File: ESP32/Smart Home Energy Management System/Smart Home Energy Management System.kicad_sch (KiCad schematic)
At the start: 154 parts, among them J1 NEPA, J10 N, J11 PZEM_SIG, J14 USB_C Conn, J15 TRANS 1-OUT, J16 128X64 GLCD, J17 TRANS-IN, J18 TRANS 2-OUT, J19 DISPLAY, J2 INVERTER, J20 LOAD 6, J21 LOAD 5, J22 LOAD 4, J23 LOAD 3, J24 LOAD 2, J25 LOAD 1, J3 CT, J6 PZEM_LOAD, K1 10A RELAY, K10 30A RELAY, K11 30A RELAY, K12 30A RELAY, K13 30A RELAY, K2 30A RELAY, K3 30A RELAY, K4 30A RELAY, K5 30A RELAY, K6 30A RELAY, K7 30A RELAY, K8 30A RELAY, K9 30A RELAY, Q1 UMH3N, Q2 UMH3N, Q3 ULN2803ADWR, Q4 ULN2803ADWR, SW1 RESET, SW2 FLASH, SW3 RotaryEncoder, T1 2220-12V, T2 2220-12V, U1 LM2596S-3.3V, U2 LM2596S-12, U3 ESP32-WROOM, U4 LM2596S-5V, U5 AMS1117-3.3, U6 PCA9555D, U7 CH340C, Y1 12MHz

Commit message: update from home
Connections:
- net D+: now reaches J14.2 (Pin_2), U7.5 (UD+)
- net D-: now reaches J14.3 (Pin_3), U7.6 (UD-)
- net RXN: no longer names the net of J11.3 (Pin_3), JP2.2 (B)
- net TXP: no longer names the net of J11.2 (Pin_2), JP1.2 (B)
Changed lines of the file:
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@@
 	)
 	(junction
-		(at 193.04 69.85)
-		(diameter 0)
-		(color 0 0 0 0)
-	)
-	(junction
 		(at 144.78 62.23)
 		(diameter 0)
@@
 	)
 	(junction
-		(at 200.66 71.12)
-		(diameter 0)
-		(color 0 0 0 0)
-	)
-	(junction
 		(at 191.77 157.48)
 		(diameter 0)
@@
 	(wire
 		(pts
-			(xy 193.04 66.04) (xy 193.04 69.85)
-		)
-		(stroke
-			(width 0)
-			(type default)
-		)
-	)
-	(wire
-		(pts
 			(xy 308.61 111.76) (xy 309.88 111.76)
 		)
@@
 	(wire
 		(pts
-			(xy 200.66 66.04) (xy 200.66 71.12)
-		)
-		(stroke
-			(width 0)
-			(type default)
-		)
-	)
-	(wire
-		(pts
 			(xy 64.77 185.42) (xy 71.12 185.42)
 		)
@@
 	(wire
 		(pts
-			(xy 209.55 261.62) (xy 209.55 271.78)
-		)
-		(stroke
-			(width 0)
-			(type default)
-		)
-	)
-	(wire
-		(pts
 			(xy 135.89 57.15) (xy 135.89 62.23)
 		)
@@
 	(wire
 		(pts
-			(xy 189.23 69.85) (xy 193.04 69.85)
+			(xy 189.23 69.85) (xy 247.65 69.85)
 		)
 		(stroke
@@
 	(wire
 		(pts
+			(xy 209.55 261.62) (xy 209.55 271.78)
+		)
+		(stroke
+			(width 0)
+			(type default)
+		)
+	)
+	(wire
+		(pts
 			(xy 180.34 172.72) (xy 180.34 185.42)
 		)
@@
 	(wire
 		(pts
-			(xy 66.04 266.7) (xy 69.85 266.7)
-		)
-		(stroke
-			(width 0)
-			(type default)
-		)
-	)
-	(wire
-		(pts
 			(xy 245.11 116.84) (xy 264.16 116.84)
 		)
@@
 	(wire
 		(pts
-			(xy 193.04 69.85) (xy 247.65 69.85)
-		)
-		(stroke
-			(width 0)
-			(type default)
-		)
-	)
-	(wire
-		(pts
 			(xy 34.29 48.26) (xy 34.29 49.53)
 		)
@@
 	(wire
 		(pts
+			(xy 62.23 266.7) (xy 69.85 266.7)
+		)
+		(stroke
+			(width 0)
+			(type default)
+		)
+	)
+	(wire
+		(pts
 			(xy 269.24 229.87) (xy 276.86 229.87)
 		)
@@
 		)
 	)
+	(label "D+"
+		(at 195.58 69.85 0)
+		(fields_autoplaced yes)
+		(effects
+			(font
+				(size 1.27 1.27)
+			)
+			(justify left bottom)
+		)
+		(property "Netclass" "DIFF"
+			(at 195.58 71.12 0)
+			(effects
+				(font
+					(size 1.27 1.27)
+					(italic yes)
+				)
+				(justify left)
+			)
+		)
+	)
 	(label "GPIO17"
 		(at 125.73 152.4 180)
@@
 		)
 	)
-	(label "RXN"
-		(at 107.95 158.75 0)
-		(effects
-			(font
-				(size 1.27 1.27)
-			)
-			(justify left bottom)
-		)
-		(property "Netclass" "DIFF"
-			(at 102.616 157.988 0)
-			(effects
-				(font
-					(size 1.27 1.27)
-					(italic yes)
-				)
-				(justify left)
-			)
-		)
-	)
 	(label "INVERTER"
 		(at 300.99 80.01 0)
@@
 	)
 	(label "N"
-		(at 66.04 266.7 0)
+		(at 62.23 266.7 0)
 		(effects
 			(font
@@
 		)
 	)
-	(label "TXP"
-		(at 107.95 156.21 0)
-		(effects
-			(font
-				(size 1.27 1.27)
-			)
-			(justify left bottom)
-		)
-		(property "Netclass" "DIFF"
-			(at 102.616 155.448 0)
-			(effects
-				(font
-					(size 1.27 1.27)
-					(italic yes)
-				)
-				(justify left)
-			)
-		)
-	)
 	(label "DTR"
 		(at 232.41 52.07 180)
@@
 		)
 	)
+	(label "D-"
+		(at 195.58 72.39 0)
+		(effects
+			(font
+				(size 1.27 1.27)
+			)
+			(justify left bottom)
+		)
+		(property "Netclass" "DIFF"
+			(at 190.5 71.374 0)
+			(effects
+				(font
+					(size 1.27 1.27)
+					(italic yes)
+				)
+				(justify left)
+			)
+		)
+	)
 	(label "CT +"
 		(at 64.77 161.29 0)
@@
 		(length 2.54)
 		(shape round)
-		(at 193.04 66.04 0)
-		(fields_autoplaced yes)
-		(effects
-			(font
-				(size 1.27 1.27)
-			)
-			(justify left bottom)
-		)
-		(property "Netclass" "DIFF"
-			(at 193.6496 63.5 0)
-			(effects
-				(font
-					(size 1.27 1.27)
-				)
-				(justify left)
-			)
-		)
-		(property "Component Class" ""
-			(at -35.56 -59.69 0)
-			(effects
-				(font
-					(size 1.27 1.27)
-					(italic yes)
-				)
-			)
-		)
-	)
-	(netclass_flag ""
-		(length 2.54)
-		(shape round)
 		(at 331.47 82.55 0)
 		(fields_autoplaced yes)
@@
 			(effects
 				(font
-					(size 1.27 1.27)
-					(italic yes)
-				)
-			)
-		)
-	)
-	(netclass_flag ""
-		(length 2.54)
-		(shape round)
-		(at 200.66 66.04 0)
-		(fields_autoplaced yes)
-		(effects
-			(font
-				(size 1.27 1.27)
-			)
-			(justify left bottom)
-		)
-		(property "Netclass" "DIFF"
-			(at 201.2696 63.5 0)
-			(effects
-				(font
-					(size 1.27 1.27)
-				)
-				(justify left)
-			)
-		)
-		(property "Component Class" ""
-			(at -27.94 -59.69 0)
-			(effects
-				(font

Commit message: update from home
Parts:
- R13: footprint Resistor_THT:R_Axial_DIN0207_L6.3mm_D2.5mm_P10.16mm_Horizontal -> Resistor_THT:R_Axial_DIN0207_L6.3mm_D2.5mm_P7.62mm_Horizontal
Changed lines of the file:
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@@
 	)
 	(junction
+		(at 215.9 21.59)
+		(diameter 0)
+		(color 0 0 0 0)
+	)
+	(junction
 		(at 331.47 175.26)
 		(diameter 0)
@@
 	)
 	(junction
+		(at 189.23 21.59)
+		(diameter 0)
+		(color 0 0 0 0)
+	)
+	(junction
 		(at 114.3 62.23)
 		(diameter 0)
@@
 	(wire
 		(pts
-			(xy 185.42 21.59) (xy 191.77 21.59)
+			(xy 185.42 21.59) (xy 189.23 21.59)
 		)
 		(stroke
@@
 	(wire
 		(pts
+			(xy 189.23 21.59) (xy 191.77 21.59)
+		)
+		(stroke
+			(width 0)
+			(type default)
+		)
+	)
+	(wire
+		(pts
 			(xy 191.77 88.9) (xy 191.77 91.44)
 		)
@@
 	(wire
 		(pts
+			(xy 215.9 17.78) (xy 215.9 21.59)
+		)
+		(stroke
+			(width 0)
+			(type default)
+		)
+	)
+	(wire
+		(pts
 			(xy 373.38 186.69) (xy 374.65 186.69)
 		)
@@
 	(wire
 		(pts
+			(xy 189.23 19.05) (xy 189.23 21.59)
+		)
+		(stroke
+			(width 0)
+			(type default)
+		)
+	)
+	(wire
+		(pts
 			(xy 139.7 22.86) (xy 144.78 22.86)
 		)
@@
 		(length 2.54)
 		(shape round)
+		(at 189.23 19.05 0)
+		(fields_autoplaced yes)
+		(effects
+			(font
+				(size 1.27 1.27)
+			)
+			(justify left bottom)
+		)
+		(property "Netclass" "PWR"
+			(at 189.8396 16.51 0)
+			(effects
+				(font
+					(size 1.27 1.27)
+				)
+				(justify left)
+			)
+		)
+		(property "Component Class" ""
+			(at 90.17 -2.54 0)
+			(effects
+				(font
+					(size 1.27 1.27)
+					(italic yes)
+				)
+			)
+		)
+	)
+	(netclass_flag ""
+		(length 2.54)
+		(shape round)
 		(at 123.19 53.34 0)
 		(fields_autoplaced yes)
@@
 		(length 2.54)
 		(shape round)
+		(at 215.9 17.78 0)
+		(fields_autoplaced yes)
+		(effects
+			(font
+				(size 1.27 1.27)
+			)
+			(justify left bottom)
+		)
+		(property "Netclass" "PWR"
+			(at 216.5096 15.24 0)
+			(effects
+				(font
+					(size 1.27 1.27)
+				)
+				(justify left)
+			)
+		)
+		(property "Component Class" ""
+			(at 116.84 -3.81 0)
+			(effects
+				(font
+					(size 1.27 1.27)
+					(italic yes)
+				)
+			)
+		)
+	)
+	(netclass_flag ""
+		(length 2.54)
+		(shape round)
 		(at 125.73 76.2 0)
 		(fields_autoplaced yes)
@@
 			)
 		)
-		(property "Footprint" "Resistor_THT:R_Axial_DIN0207_L6.3mm_D2.5mm_P10.16mm_Horizontal"
+		(property "Footprint" "Resistor_THT:R_Axial_DIN0207_L6.3mm_D2.5mm_P7.62mm_Horizontal"
 			(at 107.061 55.372 0)
 			(effects

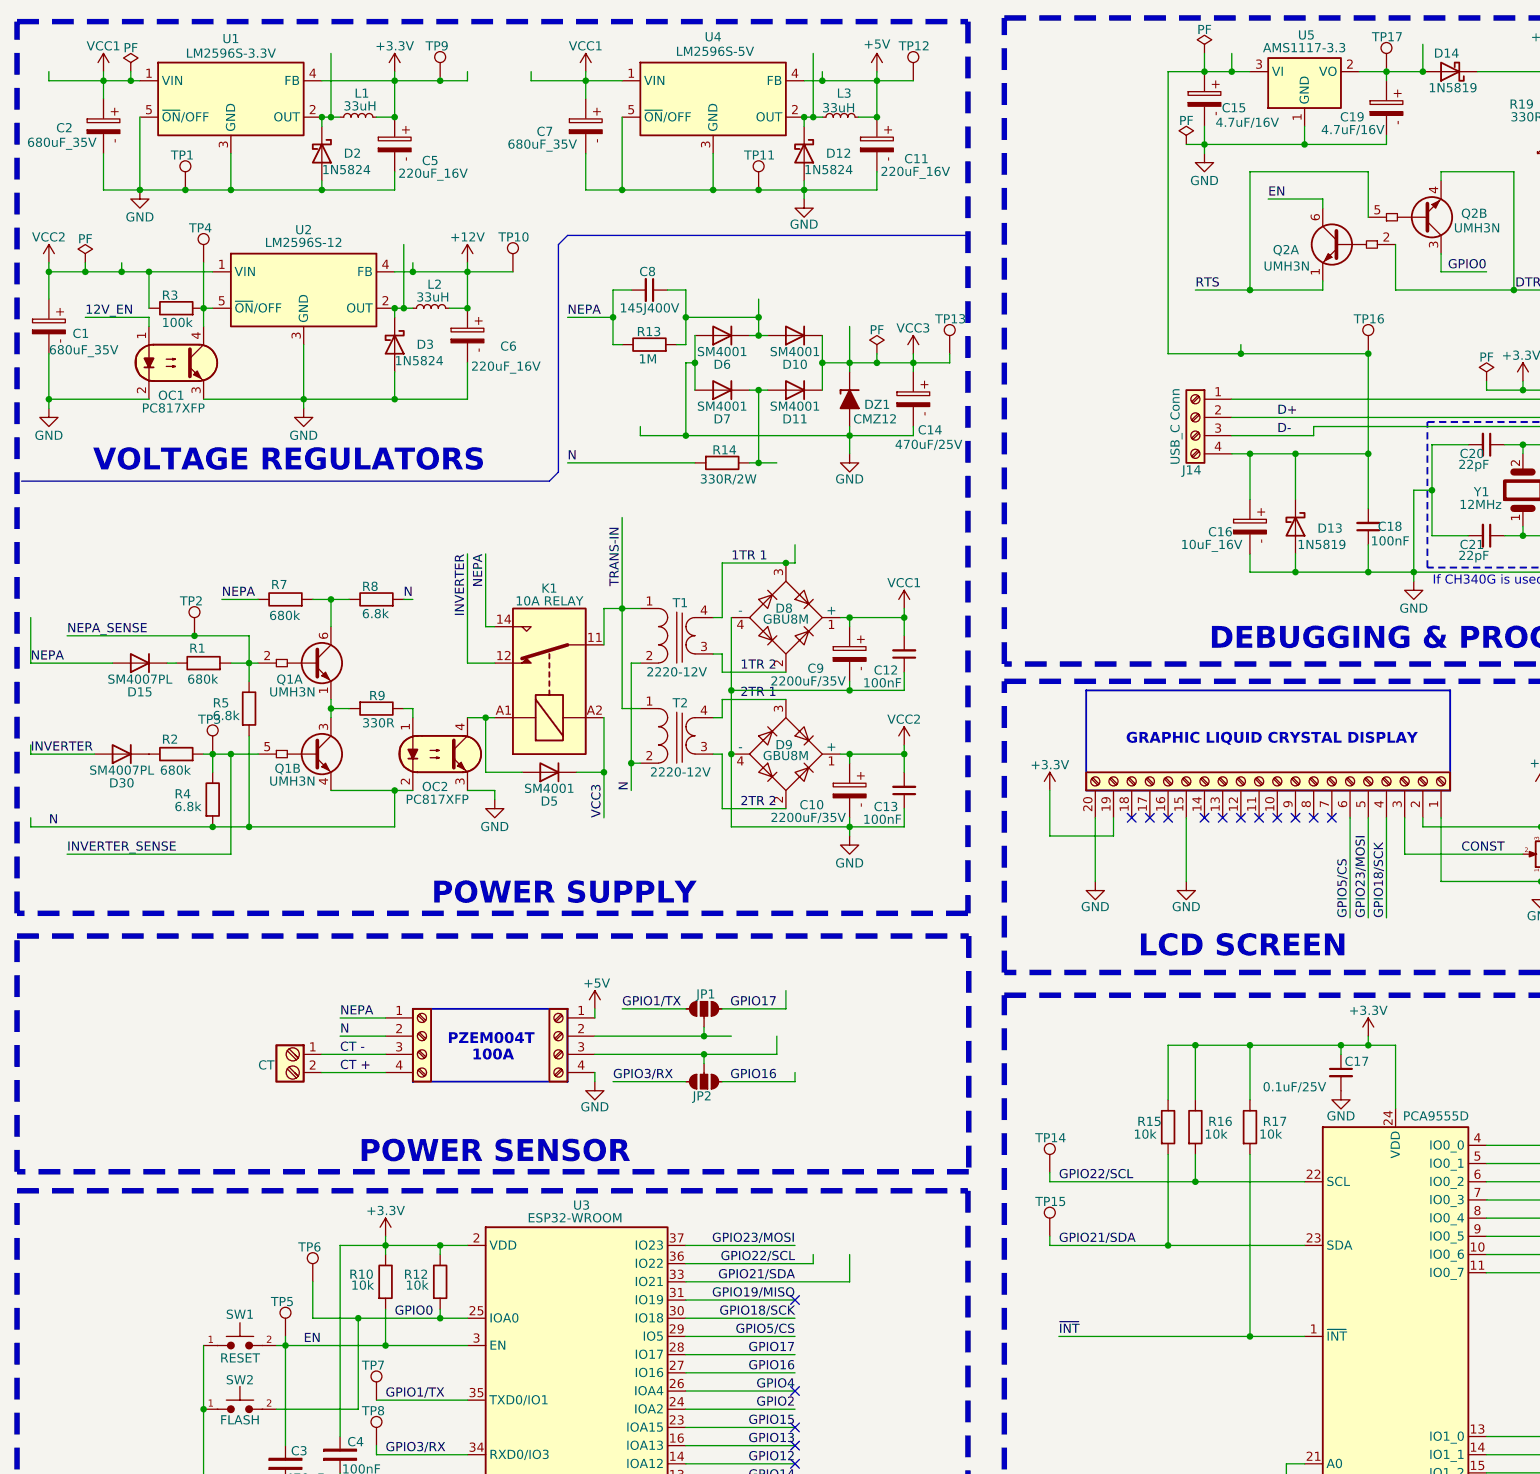
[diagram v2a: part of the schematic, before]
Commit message: Changing Blind/Buried Via into Through-hole type
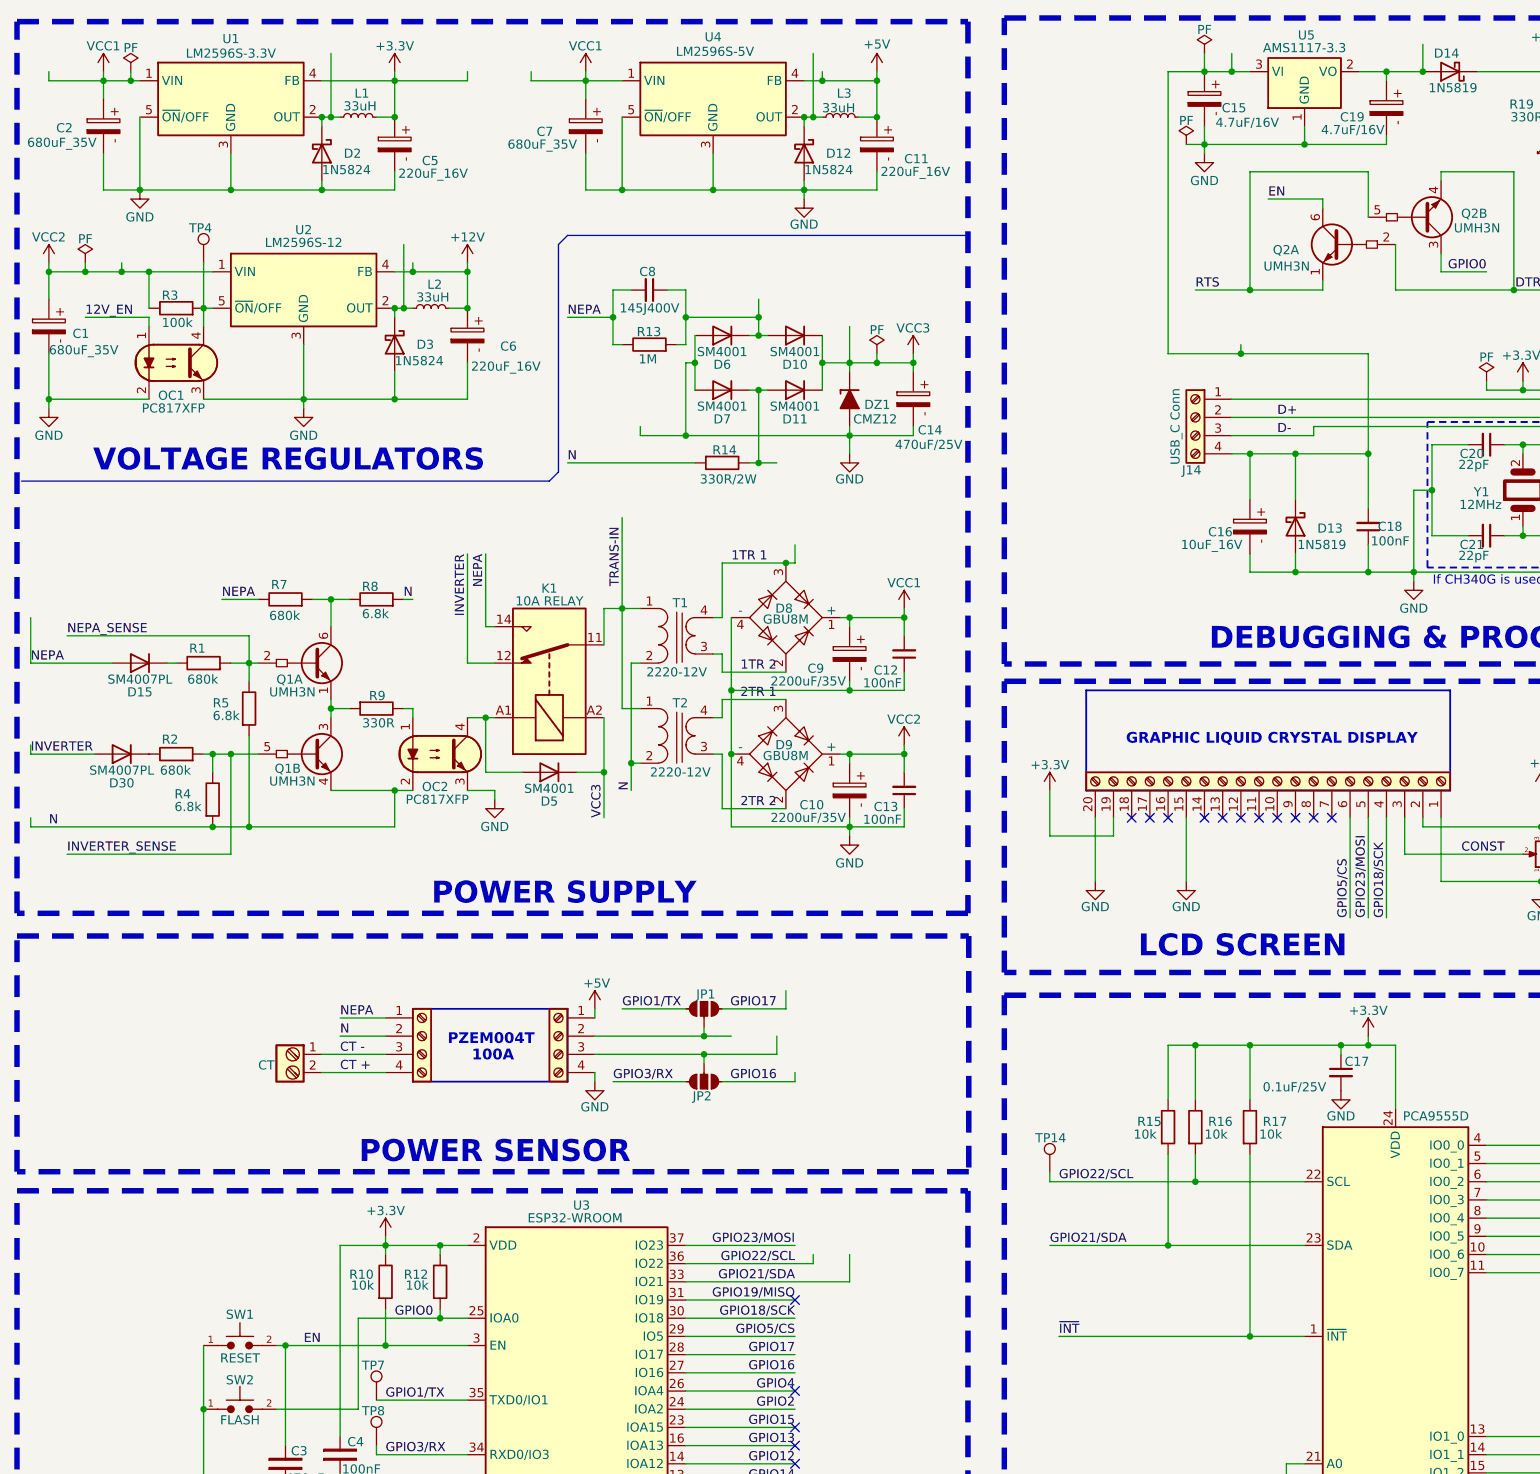
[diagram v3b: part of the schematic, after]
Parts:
- removed TP1, TP10, TP11, TP12, TP13, TP15, TP16, TP17, TP2, TP3, TP5, TP6, TP9: TestPoint, TestPoint:TestPoint_Pad_D1.5mm, symbol PCM_4ms_Connector:TestPoint
